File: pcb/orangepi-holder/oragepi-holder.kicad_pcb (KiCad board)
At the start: 2 copper layers, 1 part, among them U1 orange_pi_zero

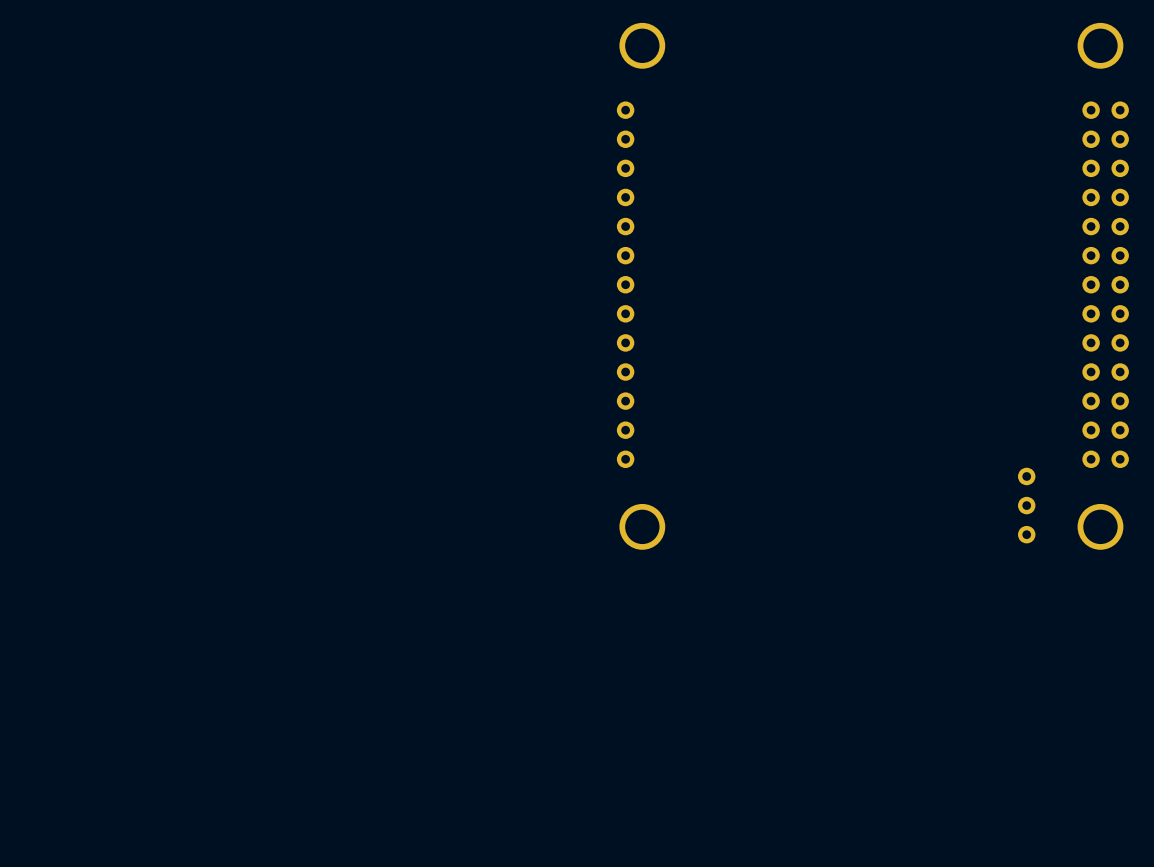
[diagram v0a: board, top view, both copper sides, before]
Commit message: Add schematic and board some development.
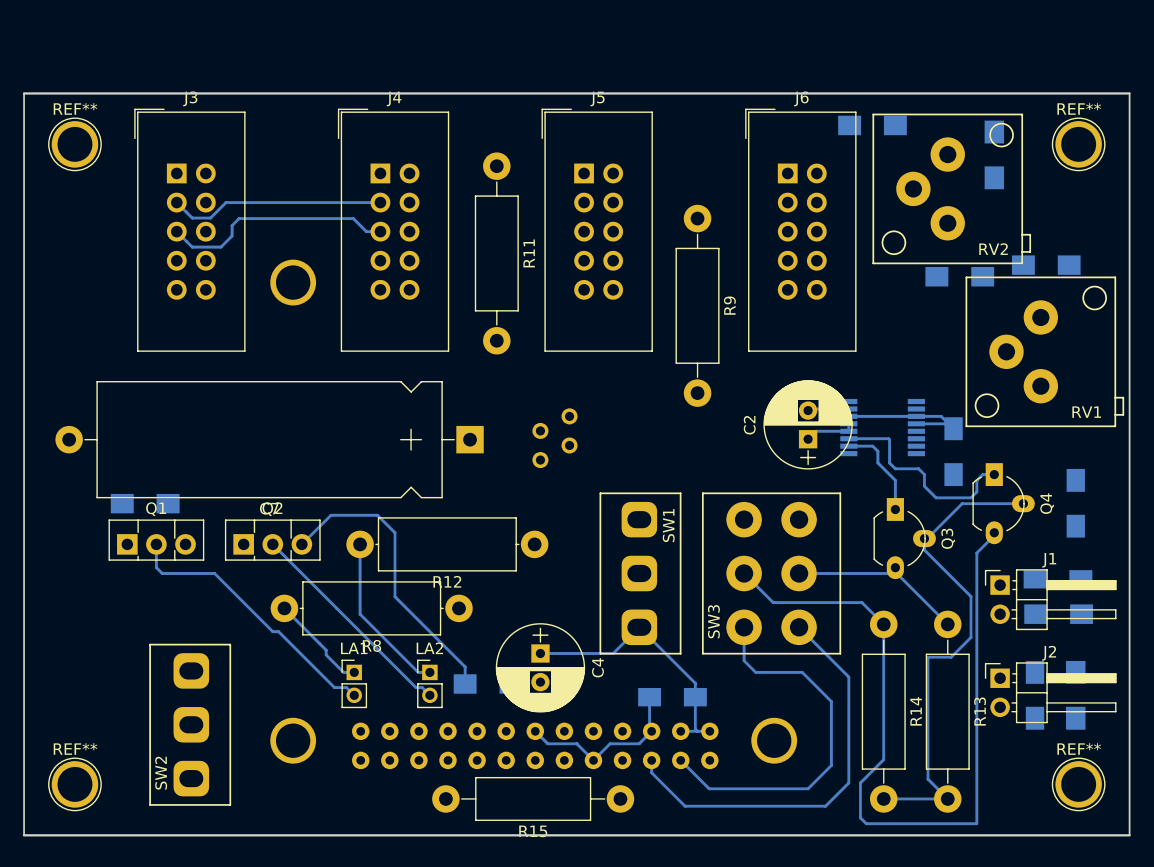
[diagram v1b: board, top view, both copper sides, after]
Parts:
- added C1: 100n, Capacitors_SMD:C_1206_HandSoldering, B.Cu at (107.2, 149.4)
- added C2: 47u, Capacitors_ThroughHole:CP_Radial_D7.5mm_P2.50mm, F.Cu at (94.5, 148.3)
- added C3: 100n, Capacitors_SMD:C_1206_HandSoldering, B.Cu at (82.6, 170.8)
- added C4: 47u, Capacitors_ThroughHole:CP_Radial_D7.5mm_P2.50mm, F.Cu at (71.1, 167.0)
- added C5: 100n, Capacitors_SMD:C_1206_HandSoldering, B.Cu at (116.3, 160.5)
- added C6: 100n, Capacitors_SMD:C_1206_HandSoldering, B.Cu at (114.3, 170.7)
- added C7: 1000u, Capacitors_ThroughHole:CP_Axial_L30.0mm_D10.0mm_P35.00mm_Horizontal, F.Cu at (65.0, 148.3)
- added C8: 100n, Capacitors_SMD:C_1206_HandSoldering, B.Cu at (117.9, 153.9)
- added J1: Conn_01x02_Male, Pin_Headers:Pin_Header_Angled_1x02_Pitch2.54mm, F.Cu at (111.3, 161.0)
- added J2: Conn_01x02_Male, Pin_Headers:Pin_Header_Angled_1x02_Pitch2.54mm, F.Cu at (111.3, 169.2)
- added J3: Conn_02x05_Odd_Even, IDC-Header:IDC-Header_2x05_P2.54mm_Vertical, F.Cu at (39.4, 125.1)
- added J4: Conn_02x05_Odd_Even, IDC-Header:IDC-Header_2x05_P2.54mm_Vertical, F.Cu at (57.1, 125.1)
- added J5: Conn_02x05_Odd_Even, IDC-Header:IDC-Header_2x05_P2.54mm_Vertical, F.Cu at (74.9, 125.1)
- added J6: Conn_02x05_Odd_Even, IDC-Header:IDC-Header_2x05_P2.54mm_Vertical, F.Cu at (92.7, 125.1)
- added J7: Conn_02x02_Odd_Even, micro-MaTch:0-215464-4_TH_4-pin_male, B.Cu at (72.4, 148.2)
- added LA1: Lamp, Pin_Headers:Pin_Header_Straight_1x02_Pitch2.00mm, F.Cu at (54.9, 168.7)
- added LA2: Lamp, Pin_Headers:Pin_Header_Straight_1x02_Pitch2.00mm, F.Cu at (61.5, 168.7)
- added Q1: BD227, TO_SOT_Packages_THT:TO-126_Vertical, F.Cu at (35.1, 157.5)
- added Q2: BD227, TO_SOT_Packages_THT:TO-126_Vertical, F.Cu at (45.2, 157.5)
- added Q3: BSN10A, TO_SOT_Packages_THT:TO-92_Molded_Wide_Oval, F.Cu at (102.1, 154.4)
- added Q4: BSN10A, TO_SOT_Packages_THT:TO-92_Molded_Wide_Oval, F.Cu at (110.7, 151.4)
- added R1: 22k, Resistors_SMD:R_1206_HandSoldering, B.Cu at (107.7, 134.1)
- added R10: 4k7, Resistors_SMD:R_1206_HandSoldering, B.Cu at (66.5, 169.7)
- added R11: 4k7, Resistors_ThroughHole:R_Axial_DIN0411_L9.9mm_D3.6mm_P15.24mm_Horizontal, F.Cu at (67.3, 124.5)
- added R12: 27, Resistors_ThroughHole:R_Axial_DIN0414_L11.9mm_D4.5mm_P15.24mm_Horizontal, F.Cu at (70.6, 157.5)
- added R13: 4k7, Resistors_ThroughHole:R_Axial_DIN0411_L9.9mm_D3.6mm_P15.24mm_Horizontal, F.Cu at (106.7, 164.5)
- added R14: 4k7, Resistors_ThroughHole:R_Axial_DIN0411_L9.9mm_D3.6mm_P15.24mm_Horizontal, F.Cu at (101.1, 164.5)
- added R15: 4k7, Resistors_ThroughHole:R_Axial_DIN0411_L9.9mm_D3.6mm_P15.24mm_Horizontal, F.Cu at (78.1, 179.7)
- added R2: 22k, Resistors_SMD:R_1206_HandSoldering, B.Cu at (100.1, 120.9)
- added R3: 22k, Resistors_SMD:R_1206_HandSoldering, B.Cu at (115.3, 133.1)
- added R4: 22k, Resistors_SMD:R_1206_HandSoldering, B.Cu at (110.7, 123.5)
- added R5: 22k, Resistors_SMD:R_1206_HandSoldering, B.Cu at (116.4, 163.6)
- added R6: 22k, Resistors_SMD:R_1206_HandSoldering, B.Cu at (117.9, 170.7)
- added R7: 4k7, Resistors_SMD:R_1206_HandSoldering, B.Cu at (36.6, 153.9)
- added R8: 27, Resistors_ThroughHole:R_Axial_DIN0414_L11.9mm_D4.5mm_P15.24mm_Horizontal, F.Cu at (64.0, 163.1)
- added R9: 4k7, Resistors_ThroughHole:R_Axial_DIN0411_L9.9mm_D3.6mm_P15.24mm_Horizontal, F.Cu at (84.8, 129.0)
- added REF**: 1pin, Connect:1pin, F.Cu at (30.5, 122.6)
- added REF**: 1pin, Connect:1pin, F.Cu at (30.5, 178.4)
- added REF**: 1pin, Connect:1pin, F.Cu at (118.1, 178.4)
- added REF**: 1pin, Connect:1pin, F.Cu at (118.1, 122.6)
- added RV1: 1k, SP5-2:SP5-2, F.Cu at (114.8, 140.7)
- added RV2: 1k, SP5-2:SP5-2, F.Cu at (106.7, 126.4)
- added SW1: SW_SPST, SPDT:SPDT, F.Cu at (77.4, 160.0)
- added SW2: SW_Push, SPDT:SPDT, F.Cu at (43.0, 173.2)
- added SW3: SW_DPDT_x2, APEM_5246:APEM_5246, F.Cu at (91.3, 160.0)
- added U2: DAC5573, Housings_SSOP:TSSOP-16_4.4x5mm_Pitch0.65mm, B.Cu at (101.0, 147.3)
- moved U1 27.1 mm to (94.5, 131.6), turned to 270 degrees
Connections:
- U1 pad 102: (no net) -> Net-(C3-Pad1)
- U1 pad 103: (no net) -> OPI_SDA
- U1 pad 104: (no net) -> Net-(C3-Pad1)
- U1 pad 105: (no net) -> OPI_SCL
- U1 pad 106: (no net) -> GND
- U1 pad 109: (no net) -> GND
- U1 pad 114: (no net) -> GND
- U1 pad 120: (no net) -> GND
- U1 pad 125: (no net) -> GND
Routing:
- net Net-(Q4-Pad3): track 0.00 -> 68.2 mm
- net +3V3: track 0.00 -> 43.4 mm
- net SDA: track 0.00 -> 37.0 mm
- net OPI_SCL: track 0.00 -> 35.7 mm
- net OPI_SDA: track 0.00 -> 32.6 mm
- net SCL: track 0.00 -> 28.8 mm
- net LAMP2: track 0.00 -> 25.6 mm
- net Net-(LA1-Pad2): track 0.00 -> 23.9 mm
- net Net-(C3-Pad1): track 0.00 -> 23.3 mm
- net Net-(LA2-Pad2): track 0.00 -> 19.2 mm
- net GND: track 0.00 -> 18.9 mm
- net +5V: track 0.00 -> 18.2 mm
- net Net-(Q3-Pad3): track 0.00 -> 15.5 mm
- net Net-(LA2-Pad1): track 0.00 -> 14.3 mm
- net Net-(LA1-Pad1): track 0.00 -> 8.65 mm
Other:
- board outline added: 96.5 x 64.8 mm

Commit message: Finished schematic and pcb for orange pi.
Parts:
- J7: moved to F.Cu
- moved R15 52.6 mm to (31.1, 156.1), turned to 270 degrees
- moved R7 17.8 mm to (46.6, 168.7)
- moved R2 12.3 mm to (102.1, 133.1), turned to 90 degrees
- moved R4 9.25 mm to (101.5, 123.1), turned to 0 degrees
- moved C8 5.83 mm to (112.0, 153.4), turned to 0 degrees
- moved Q4 4.10 mm to (107.2, 153.4)
- moved C4 2.90 mm to (72.7, 169.4), turned to 180 degrees
- moved R5 2.27 mm to (114.4, 162.4), turned to 270 degrees
- moved C5 2.09 mm to (117.2, 162.4), turned to 90 degrees
- moved R10 2.02 mm to (66.8, 167.7), turned to 270 degrees
- moved J7 1.92 mm to (74.3, 148.0), turned to 270 degrees
- moved C1 1.79 mm to (108.9, 149.0), turned to 0 degrees
- moved R9 1.63 mm to (83.8, 127.8)
- moved SW3 1.52 mm to (91.3, 161.5)
- moved Q3 1.52 mm to (100.6, 154.4)
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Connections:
- J7 pad 2: +5V -> GND
- J7 pad 4: GND -> +3V3
- R15 pad 1: (no net) -> +3V3
- SW3 pad 1: Net-(J7-Pad3) -> Net-(J7-Pad1)
- SW3 pad 4: Net-(J7-Pad1) -> Net-(J7-Pad3)
- U1 pad 107: (no net) -> BUTTON
- U1 pad 116: (no net) -> LAMP2
- U1 pad 122: (no net) -> LAMP1
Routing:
- net +3V3: track 43.4 -> 200.0 mm, vias 0 -> 2
- net +5V: track 18.2 -> 156.6 mm, vias 0 -> 4
- net SCL: track 28.8 -> 109.2 mm
- net SDA: track 37.0 -> 116.5 mm
- net GND: track 18.9 -> 80.8 mm, vias 0 -> 2
- net BUTTON: track 0.00 -> 58.6 mm
- net Net-(C6-Pad2): track 0.00 -> 57.1 mm
- net LAMP1: track 0.00 -> 40.4 mm
- net Net-(J7-Pad3): track 0.00 -> 24.3 mm
- net Net-(C5-Pad2): track 0.00 -> 24.3 mm
- net Net-(J7-Pad1): track 0.00 -> 17.2 mm
- net Net-(R2-Pad1): track 0.00 -> 13.0 mm
- net Net-(R1-Pad1): track 0.00 -> 12.4 mm
- net Net-(R2-Pad2): track 0.00 -> 9.08 mm
- net Net-(R3-Pad2): track 0.00 -> 8.48 mm
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- added copper zone on B.Cu, net GND
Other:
- board text added: "2018"
- board text added: "Michał"
- board text added: "Słomkowski"

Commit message: Final orange pi board.
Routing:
- net +3V3: track 200.0 -> 200.7 mm
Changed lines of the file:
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@@
     (thickness 1.6)
     (drawings 7)
-    (tracks 416)
+    (tracks 417)
     (zones 0)
     (modules 47)
@@
   )
   (setup
-    (last_trace_width 1)
+    (last_trace_width 2)
     (user_trace_width 0.4)
     (user_trace_width 0.5)
@@
   (segment (start 73.025 144.78) (end 68.58 144.78) (width 1.2) (layer B.Cu) (net 6))
   (segment (start 68.58 144.78) (end 65.151 141.478) (width 1.2) (layer B.Cu) (net 6))
+  (segment (start 73.025 146.05) (end 73.025 145.288) (width 1.5) (layer B.Cu) (net 6))
   (segment (start 40.646399 128.898601) (end 40.233599 129.311401) (width 0.4) (layer B.Cu) (net 7))
   (segment (start 40.233599 129.311401) (end 39.37 130.175) (width 0.4) (layer B.Cu) (net 7))
@@
   (segment (start 81.013202 124.968) (end 79.622601 126.358601) (width 1.2) (layer B.Cu) (net 8))
   (segment (start 85.598 124.968) (end 81.013202 124.968) (width 1.2) (layer B.Cu) (net 8))
-  (segment (start 93.726 156.844) (end 93.726 155.702) (width 1.5) (layer B.Cu) (net 9))
-  (segment (start 93.726 155.702) (end 92.456 154.432) (width 1.5) (layer B.Cu) (net 9))
+  (segment (start 93.726 156.844) (end 93.726 155.702) (width 2) (layer B.Cu) (net 9))
+  (segment (start 93.726 155.702) (end 92.456 154.432) (width 2) (layer B.Cu) (net 9))
   (segment (start 92.456 154.432) (end 91.694 153.67) (width 0.8) (layer B.Cu) (net 9))
   (segment (start 91.694 153.67) (end 86.106 153.67) (width 0.8) (layer B.Cu) (net 9))
@@
   (segment (start 79.502 152.4) (end 77.851 150.749) (width 0.8) (layer B.Cu) (net 9))
   (segment (start 77.851 150.749) (end 77.851 148.082) (width 1) (layer B.Cu) (net 9))
-  (segment (start 77.089 147.32) (end 75.565 147.32) (width 1) (layer B.Cu) (net 9))
+  (segment (start 77.089 147.32) (end 75.565 147.32) (width 2) (layer B.Cu) (net 9))
   (segment (start 77.851 148.082) (end 77.089 147.32) (width 1) (layer B.Cu) (net 9))
-  (segment (start 88.926 156.844) (end 85.47 156.844) (width 1.5) (layer B.Cu) (net 10))
+  (segment (start 88.926 156.844) (end 85.47 156.844) (width 2) (layer B.Cu) (net 10))
   (segment (start 85.47 156.844) (end 83.82 155.194) (width 1.5) (layer B.Cu) (net 10))
   (segment (start 83.82 155.194) (end 82.55 153.924) (width 0.8) (layer B.Cu) (net 10))
   (segment (start 82.55 153.924) (end 77.978 153.924) (width 0.8) (layer B.Cu) (net 10))
   (segment (start 77.978 153.924) (end 75.565 151.511) (width 0.8) (layer B.Cu) (net 10))
-  (segment (start 75.565 151.511) (end 75.565 149.86) (width 1) (layer B.Cu) (net 10))
+  (segment (start 75.565 151.511) (end 75.565 149.86) (width 2) (layer B.Cu) (net 10))
   (segment (start 53.909406 170.148) (end 53.877406 170.18) (width 0.8) (layer B.Cu) (net 11))
   (segment (start 54.864 170.148) (end 53.909406 170.148) (width 1) (layer B.Cu) (net 11))
@@
   (segment (start 105.156 164.084) (end 100.584 159.512) (width 1.5) (layer B.Cu) (net 17))
   (segment (start 105.156 164.465) (end 105.156 164.084) (width 1.5) (layer B.Cu) (net 17))
-  (segment (start 93.726 161.544) (end 95.377 161.544) (width 1.5) (layer B.Cu) (net 17))
+  (segment (start 93.726 161.544) (end 95.377 161.544) (width 2) (layer B.Cu) (net 17))
   (segment (start 97.409 159.512) (end 100.584 159.512) (width 1.5) (layer B.Cu) (net 17))
   (segment (start 95.377 161.544) (end 97.409 159.512) (width 1.5) (layer B.Cu) (net 17))
@@
   (segment (start 94.234 169.418) (end 96.266 171.45) (width 1.2) (layer B.Cu) (net 27))
   (segment (start 91.405969 169.418) (end 89.662 169.418) (width 1.2) (layer B.Cu) (net 27))
-  (segment (start 88.926 168.682) (end 88.926 166.244) (width 1.2) (layer B.Cu) (net 27))
+  (segment (start 88.926 168.682) (end 88.926 166.244) (width 2) (layer B.Cu) (net 27))
   (segment (start 89.662 169.418) (end 88.926 168.682) (width 1.2) (layer B.Cu) (net 27))
   (zone (net 2) (net_name GND) (layer B.Cu) (hatch edge 0.508)

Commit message: Update part values.
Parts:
- R11, R13, R14, R9: value 4k7 -> 3k6
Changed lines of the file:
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@@
   )
   (setup
-    (last_trace_width 2)
+    (last_trace_width 0.25)
     (user_trace_width 0.4)
     (user_trace_width 0.5)
@@
       (effects (font (size 1 1) (thickness 0.15)))
     )
-    (fp_text value 4k7 (at 7.62 2.86 270) (layer F.Fab)
+    (fp_text value 3k6 (at 7.62 2.86 270) (layer F.Fab)
       (effects (font (size 1 1) (thickness 0.15)))
     )
@@
       (effects (font (size 1 1) (thickness 0.15)))
     )
-    (fp_text value 4k7 (at 7.62 2.86 270) (layer F.Fab)
+    (fp_text value 3k6 (at 7.62 2.86 270) (layer F.Fab)
       (effects (font (size 1 1) (thickness 0.15)))
     )
@@
       (effects (font (size 1 1) (thickness 0.15)))
     )
-    (fp_text value 4k7 (at 7.62 2.86 270) (layer F.Fab)
+    (fp_text value 3k6 (at 7.62 2.86 270) (layer F.Fab)
       (effects (font (size 1 1) (thickness 0.15)))
     )
@@
       (effects (font (size 1 1) (thickness 0.15)))
     )
-    (fp_text value 4k7 (at 7.62 2.86 270) (layer F.Fab)
-      (effects (font (size 1 1) (thickness 0.15)))
-    )
+    (fp_text value 3k6 (at 7.62 2.86 270) (layer F.Fab)
+      (effects (font (size 1 1) (thickness 0.15)))
+    )

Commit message: Update all Kicad files to Kicad 5.
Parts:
- R13, R14: value 3k6 -> 10k
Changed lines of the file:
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@@
       (effects (font (size 1 1) (thickness 0.15)))
     )
-    (fp_text value 3k6 (at 7.62 2.86 270) (layer F.Fab)
+    (fp_text value 10k (at 7.62 2.86 270) (layer F.Fab)
       (effects (font (size 1 1) (thickness 0.15)))
     )
@@
       (effects (font (size 1 1) (thickness 0.15)))
     )
-    (fp_text value 3k6 (at 7.62 2.86 270) (layer F.Fab)
+    (fp_text value 10k (at 7.62 2.86 270) (layer F.Fab)
       (effects (font (size 1 1) (thickness 0.15)))
     )

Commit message: Migrate to KiCAD 9.
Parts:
- R1, R2, R3, R4: value 22k -> 1k
- R5, R6: value 22k -> 470
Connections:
- J3 pad 4: (no net) -> unconnected-(J3-Pin_4-Pad4)
- J3 pad 6: (no net) -> unconnected-(J3-Pin_6-Pad6)
- J3 pad 7: (no net) -> unconnected-(J3-Pin_7-Pad7)
- J4 pad 4: (no net) -> unconnected-(J4-Pin_4-Pad4)
- J4 pad 6: (no net) -> unconnected-(J4-Pin_6-Pad6)
- J4 pad 7: (no net) -> unconnected-(J4-Pin_7-Pad7)
- J5 pad 4: (no net) -> unconnected-(J5-Pin_4-Pad4)
- J5 pad 6: (no net) -> unconnected-(J5-Pin_6-Pad6)
- J5 pad 7: (no net) -> unconnected-(J5-Pin_7-Pad7)
- J6 pad 4: (no net) -> unconnected-(J6-Pin_4-Pad4)
- J6 pad 6: (no net) -> unconnected-(J6-Pin_6-Pad6)
- J6 pad 7: (no net) -> unconnected-(J6-Pin_7-Pad7)
- U1 pad 101: (no net) -> unconnected-(U1-3.3V-Pad101)
- U1 pad 108: (no net) -> unconnected-(U1-UART1_TX_/_PG06-Pad108)
- U1 pad 110: (no net) -> unconnected-(U1-UART1_RX_/_PG07-Pad110)
- U1 pad 111: (no net) -> unconnected-(U1-UART2_RX_/_PA01-Pad111)
- U1 pad 112: (no net) -> unconnected-(U1-SIM_CLK/PA_EINT7_/_PA07-Pad112)
- U1 pad 113: (no net) -> unconnected-(U1-UART2_TX_/_PA00-Pad113)
- U1 pad 115: (no net) -> unconnected-(U1-_UART2_CTS_/_PA03-Pad115)
- U1 pad 117: (no net) -> unconnected-(U1-3.3V-Pad117)
- U1 pad 118: (no net) -> unconnected-(U1-TWI1-SCK_/_PA18-Pad118)
- U1 pad 119: (no net) -> unconnected-(U1-SPI1_MOSI_/_PA15-Pad119)
- U1 pad 121: (no net) -> unconnected-(U1-SPI1_MISO_/_PA16-Pad121)
- U1 pad 123: (no net) -> unconnected-(U1-SPI1_CLK_/_PA14-Pad123)
- U1 pad 124: (no net) -> unconnected-(U1-PI1_CS_/_PA13-Pad124)
- U1 pad 126: (no net) -> unconnected-(U1-SIM_DET/PA_EINT10_/_PA10-Pad126)
- U2 pad 7: (no net) -> unconnected-(U2-VoutC-Pad7)
- U2 pad 8: (no net) -> unconnected-(U2-VoutD-Pad8)
- U2 pad 9: (no net) -> unconnected-(U2-LDAC-Pad9)
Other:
- net class Default removed
